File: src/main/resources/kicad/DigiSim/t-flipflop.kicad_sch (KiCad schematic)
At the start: 19 parts

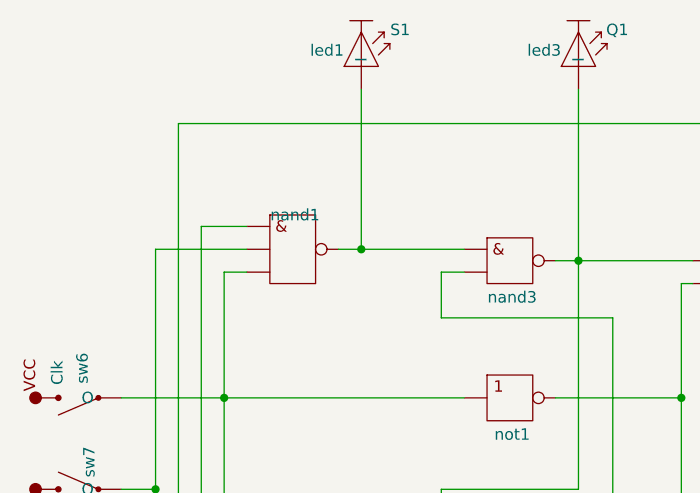
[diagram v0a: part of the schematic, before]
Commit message: Hierarchical Scheme added
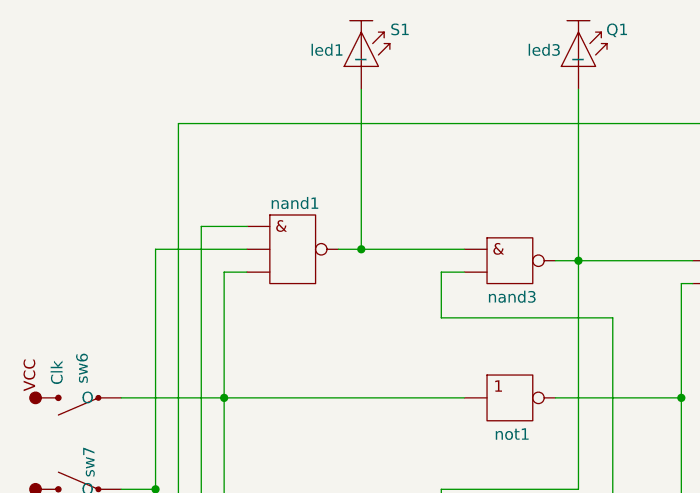
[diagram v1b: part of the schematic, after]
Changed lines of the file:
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@@
 		(dnp no)
 		(property "Reference" "nand1"
-			(at 100.584 60.96 0)
+			(at 100.584 59.69 0)
 			(show_name no)
 			(do_not_autoplace no)
